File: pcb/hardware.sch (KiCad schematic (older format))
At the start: 7 parts, among them J1 Micro_SD_Card_Det_Hirose_DM3AT, U2 A33

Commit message: Finished connecting up the RAM
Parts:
- removed unit 4 of U2
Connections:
- net ram/!LDQS: now also U2.K1 (DQS0B)
- net ram/!UDQS: now also U2.R1 (DQS1)
- net ram/LDM: now also U2.N2 (DQM0)
- net ram/LDQS: now also U2.K2 (DQS0)
- net ram/UDM: now also U2.T3 (DQM1)
- net ram/UDQS: now also U2.T1 (DQS1B)
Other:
- moved on the sheet: U2B

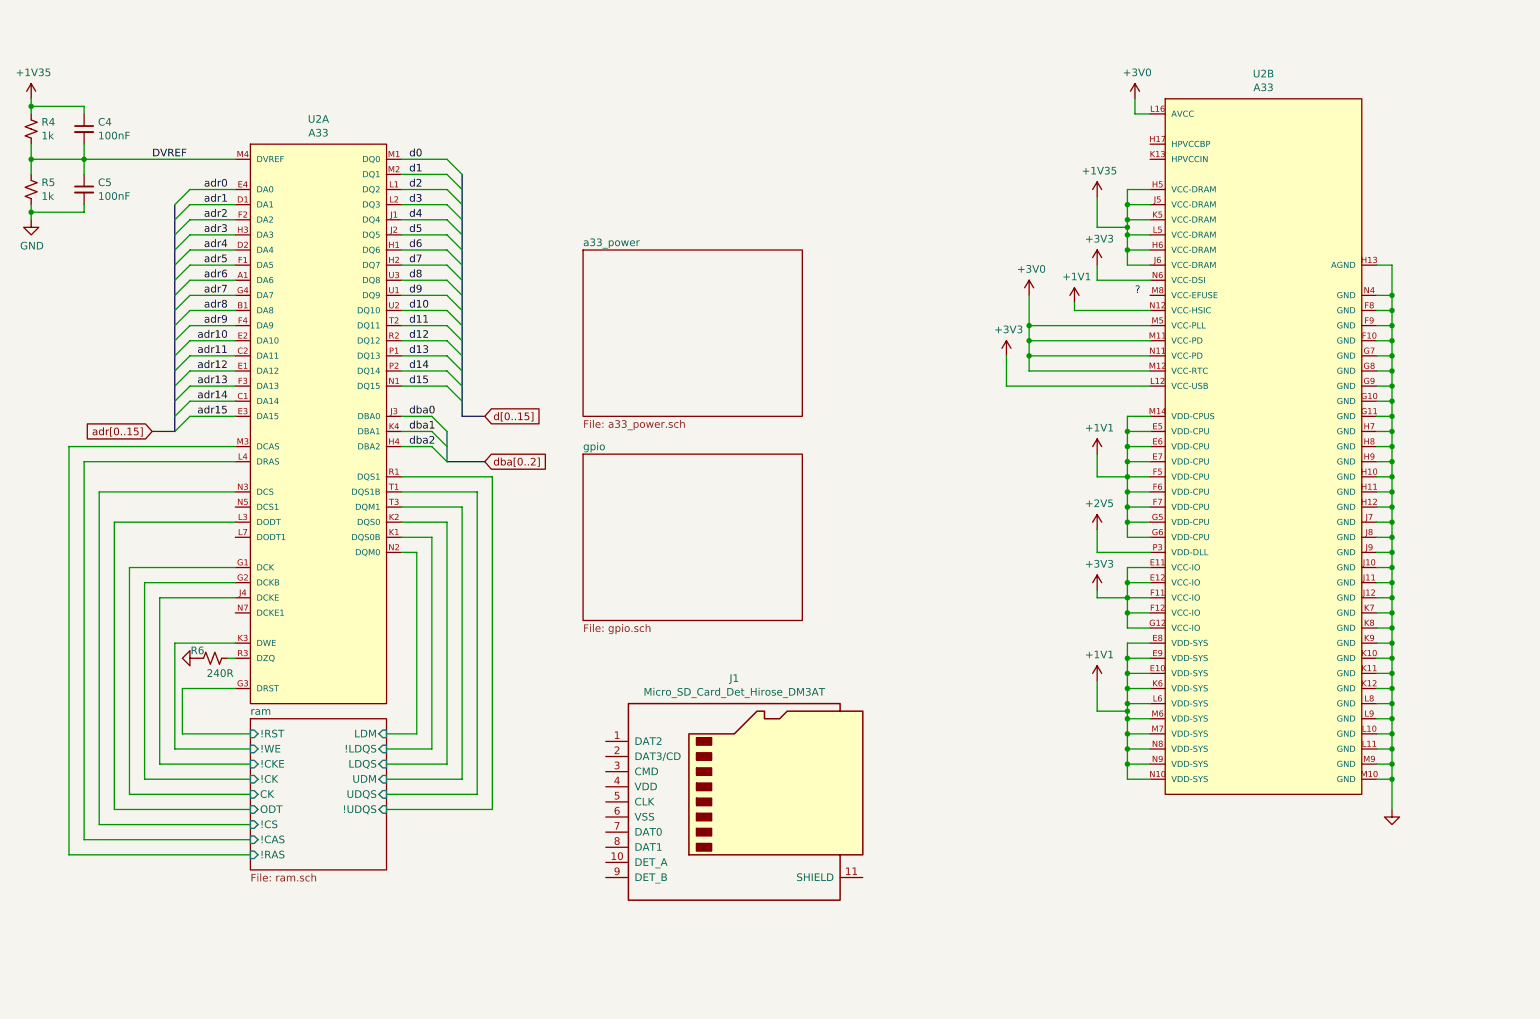
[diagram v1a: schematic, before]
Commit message: Added the 2.5V LDO
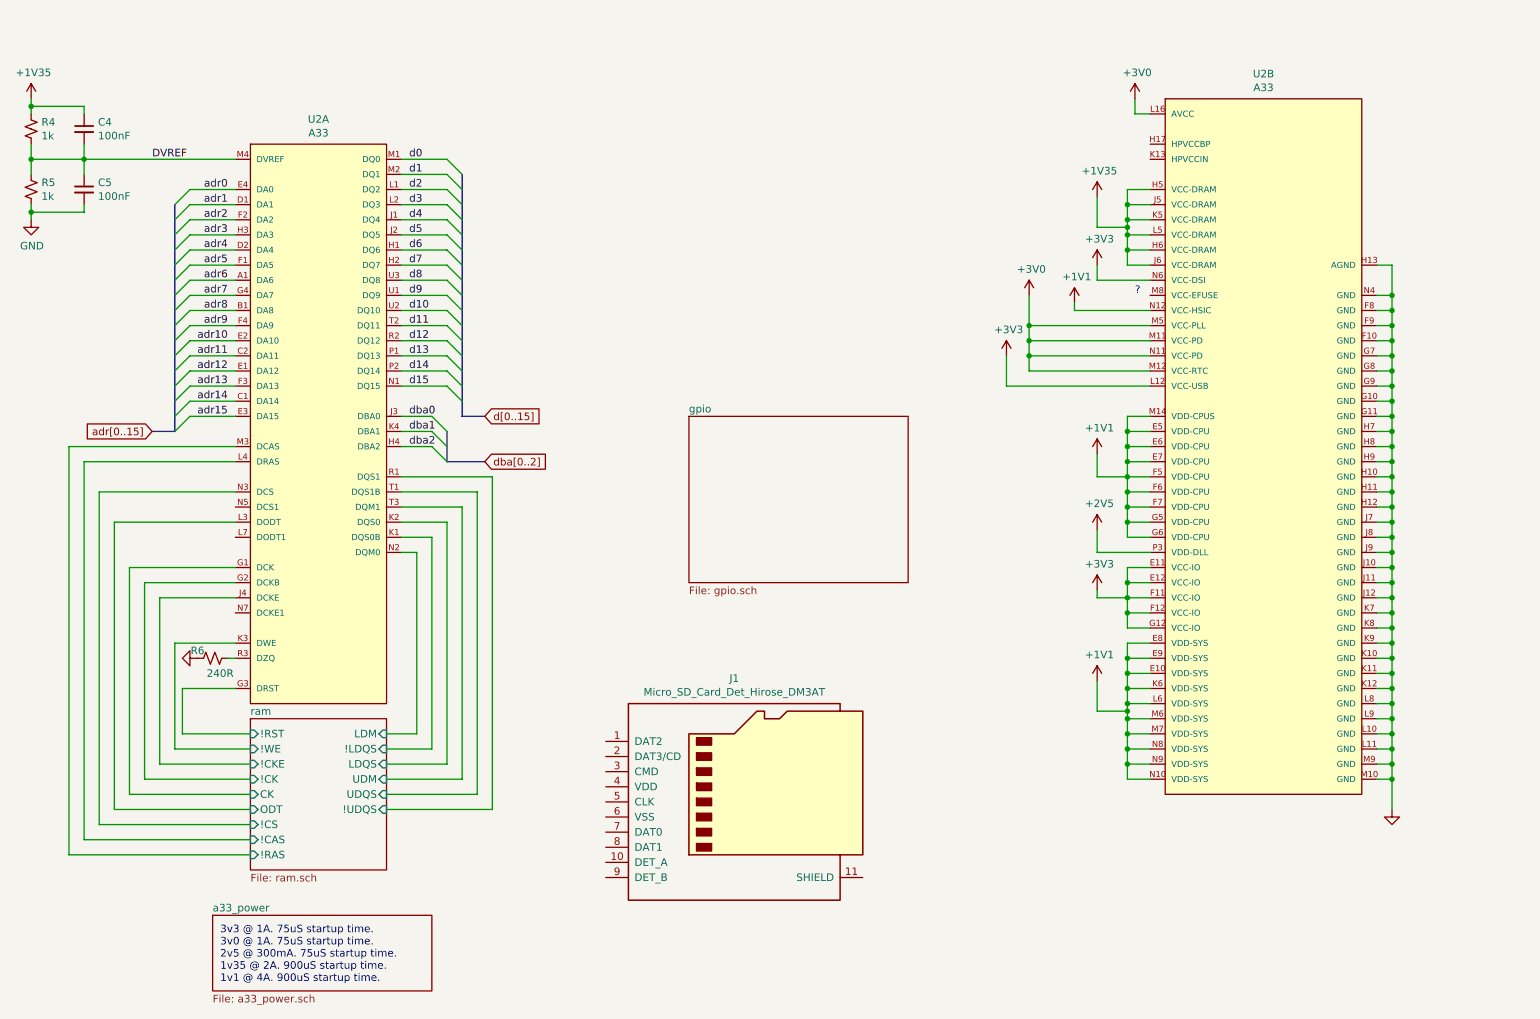
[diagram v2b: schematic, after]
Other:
- note added: "3v3 @ 1A. 75uS startup time.\n3v0 @ 1A. 75uS startup time.\n2v5 @ 300mA. 75uS startup time.\n1v35 @ 2A. 900uS startup time.\n1v1 @ 4A. 900uS startup time."
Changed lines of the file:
@@
 adr14
 $Sheet
-S 4850 3550 1450 1100
+S 5550 3300 1450 1100
 U 6063BE69
 F0 "gpio" 50
@@
 	1450 6200 2650 6200
 $Sheet
-S 4850 2200 1450 1100
+S 2400 6600 1450 500
 U 60A30BFF
 F0 "a33_power" 50
@@
 P 7650 2900
 AR Path="/60A30BFF/608815B4" Ref="#PWR?"  Part="1"
-AR Path="/608815B4" Ref="#PWR?"  Part="1"
-F 0 "#PWR?" H 7650 2750 50  0001 C CNN
+AR Path="/608815B4" Ref="#PWR043"  Part="1"
+F 0 "#PWR043" H 7650 2750 50  0001 C CNN
 F 1 "+3V3" H 7665 3073 50  0000 C CNN
 F 2 "" H 7650 2900 50  0001 C CNN
@@
 Wire Wire Line
 	3650 3700 4250 3700
+Text Notes 2450 7050 0    50   ~ 0
+3v3 @ 1A. 75uS startup time.\n3v0 @ 1A. 75uS startup time.\n2v5 @ 300mA. 75uS startup time.\n1v35 @ 2A. 900uS startup time.\n1v1 @ 4A. 900uS startup time.
 Wire Bus Line
 	3950 3400 3950 3600
